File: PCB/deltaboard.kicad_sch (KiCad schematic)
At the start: 316 parts, among them J1 USB_C_Receptacle, J2 Conn_01x04, K1 Esc, K10 F9, K11 F10, K12 F11, K13 F12, K14 Blank, K15 Blank, K16 ~~,`, K17 !,1, K18 @,2, K19 #,3, K2 F1, K20 $,4, K21 %,5, K22 ^,6, K23 &,7, K24 *,8, K25 (,9, K26 ),0, K27 _,-, K28 +,=, K29 Backspace, K3 F2, K30 Insert, K31 Home, K33 Tab, K34 Q, K35 W, K36 E, K37 R, K38 T, K39 Y, K4 F3, K40 U, K41 I, K42 O, K43 P, K44 {,[, K45 },], K46 |,\, K47 Delete, K48 End, K49 PgUp, K5 F4, K50 Caps Lock, K51 A, K52 S, K53 D, K54 F, K55 G, K56 H, K57 J, K58 K, K59 L, K6 F5, K60 :,;, K61 ",', K62 Enter, K63 Shift, K64 Z, K65 X, K66 C, K67 V, K68 B, K69 N, K7 F6, K70 M, K71 <,,, K72 >,., K73 ?,/, K74 Shift, K75 ↑, K76 Ctrl, K77 Win, K78 Alt, K79 Blank, K8 F7, K80 Alt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

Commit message: chore: add i2c pull up resistors and make vcc traces thicker
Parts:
- added R10, R7: 10k, Resistor_SMD:R_0805_2012Metric, symbol Device:R
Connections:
- net +3V3: now also R10.2, R7.2
- net I2C_SCL: now also R10.1
- net I2C_SDA: now also R7.1

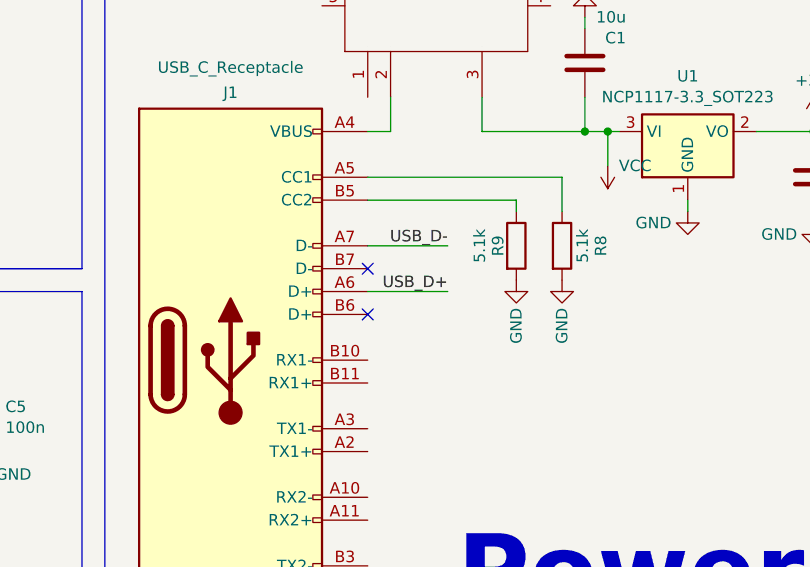
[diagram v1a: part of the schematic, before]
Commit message: chore: properly connect DN/DP
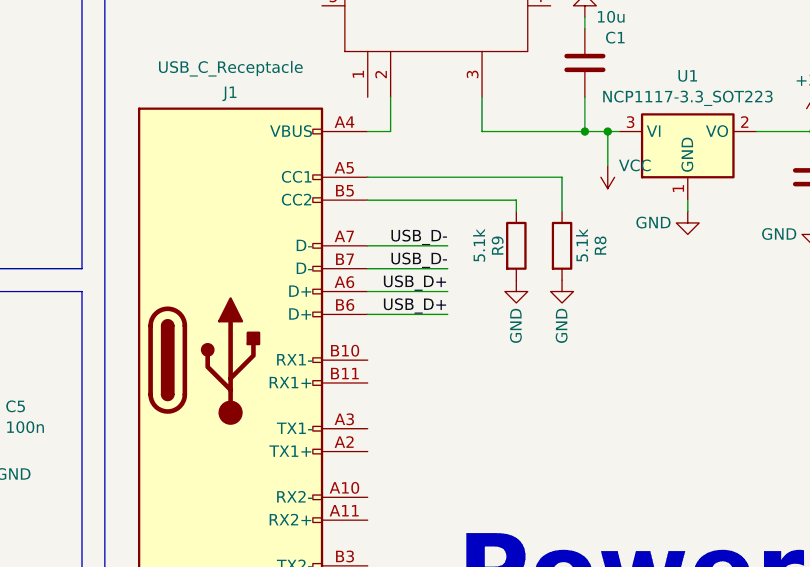
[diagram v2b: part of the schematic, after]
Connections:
- net USB_D+: now also J1.B6 (D+)
- net USB_D-: now also J1.B7 (D-)
- no-connect marks 2 -> 0
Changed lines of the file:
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@@
 		(color 0 0 0 0)
 	)
-	(no_connect
-		(at 521.97 78.74)
-	)
-	(no_connect
-		(at 521.97 83.82)
-	)
 	(wire
 		(pts
@@
 	(wire
 		(pts
+			(xy 521.97 78.74) (xy 530.86 78.74)
+		)
+		(stroke
+			(width 0)
+			(type default)
+		)
+	)
+	(wire
+		(pts
 			(xy 513.08 298.45) (xy 528.32 298.45)
 		)
@@
 	(wire
 		(pts
+			(xy 521.97 83.82) (xy 530.86 83.82)
+		)
+		(stroke
+			(width 0)
+			(type default)
+		)
+	)
+	(wire
+		(pts
 			(xy 434.34 114.3) (xy 438.15 114.3)
 		)
@@
 		)
 	)
+	(label "USB_D+"
+		(at 530.86 83.82 180)
+		(effects
+			(font
+				(size 1.27 1.27)
+			)
+			(justify right bottom)
+		)
+	)
 	(label "ROW_3"
 		(at 196.85 104.14 0)
@@
 		(effects
 			(font
+				(size 1.27 1.27)
+			)
+			(justify right bottom)
+		)
+	)
+	(label "USB_D-"
+		(at 530.86 78.74 180)
+		(effects
+			(font

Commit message: feat: optimize traces, component placement, silkscreen, etc
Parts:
- removed JP1, JP2: Jumper_2_Open, Jumper:SolderJumper-2_P1.3mm_Open_TrianglePad1.0x1.5mm, symbol Jumper:Jumper_2_Open
- added TP_BOOT1, TP_GND1, TP_RST1: TestPoint, TestPoint:TestPoint_Pad_1.5x1.5mm, symbol Connector:TestPoint
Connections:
- net GND: now also SW11.MP, TP_GND1.1
- net ~{USB_BOOT}: now also TP_BOOT1.1
- net at R6.1: now also TP_RST1.1

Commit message: feat: rework component placement + use different vrm fix bugs
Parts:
- removed TP_BOOT1, TP_RST1: TestPoint, TestPoint:TestPoint_Pad_1.5x1.5mm, symbol Connector:TestPoint
- removed U1: NCP1117-3.3_SOT223, Package_TO_SOT_SMD:SOT-223-3_TabPin2, symbol Regulator_Linear:NCP1117-3.3_SOT223
- added D88: PRTR5V0U2X, Package_TO_SOT_SMD:SOT-143, symbol Power_Protection:PRTR5V0U2X
- added J3: Conn_01x06, Connector_PinHeader_2.54mm:PinHeader_1x06_P2.54mm_Vertical, symbol Connector_Generic:Conn_01x06
- added U1: AP2112K-3.3, Package_TO_SOT_SMD:SOT-23-5, symbol Regulator_Linear:AP2112K-3.3
- R6: value 1k -> 10k
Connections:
- net GPIO28_ADC2 is gone; now on net COL_10: U3.40 (GPIO28_ADC2)
- net +3V3: now also R6.1, J3.1 (Pin_1), U1.5 (VOUT)
- net COL_10: no longer U3.27 (GPIO16)
- net GND: now also D88.1 (GND), J3.2 (Pin_2), U1.2 (GND)
- net RUN: now also J3.3 (Pin_3)
- net SWCLK: now also J3.5 (Pin_5)
- net SWD: now also J3.6 (Pin_6)
- net USB_D+: now also D88.3 (I/O2)
- net USB_D-: now also D88.2 (I/O1)
- net VCC: now also U1.1 (VIN), U1.3 (EN)
- net ~{USB_BOOT}: now also J3.4 (Pin_4)
- net VBUS_RAW: now reaches J1.A4 (VBUS), J1.A9 (VBUS), J1.B4 (VBUS), J1.B9 (VBUS), SW1.2
- net VBUS_RAW: now also D88.4 (VCC)
- new net GPIO16: U3.27 (GPIO16)
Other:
- moved on the sheet: R6

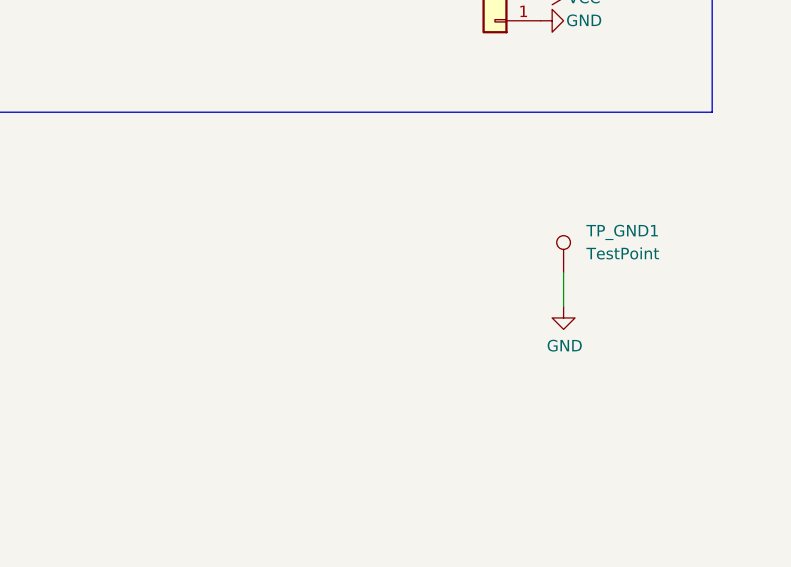
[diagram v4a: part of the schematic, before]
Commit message: feat: hide footprint text for switches
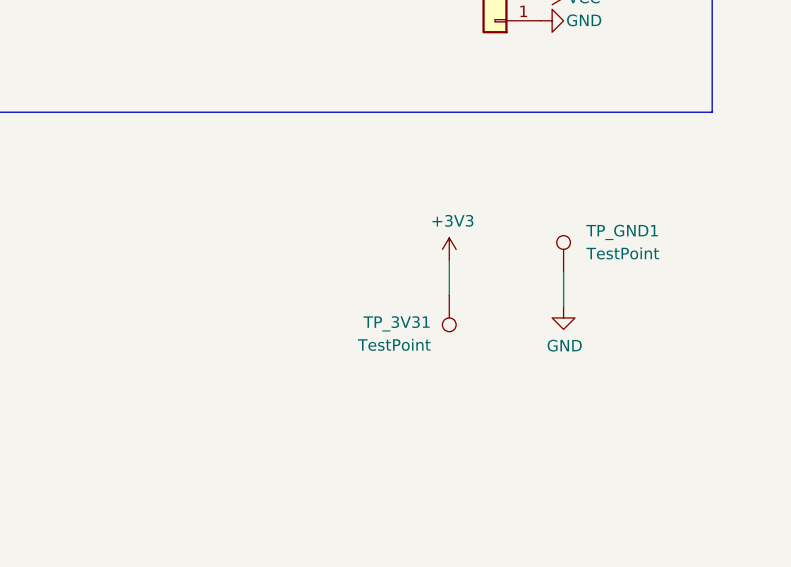
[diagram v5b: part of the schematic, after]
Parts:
- added TP_3V31: TestPoint, TestPoint:TestPoint_Pad_1.5x1.5mm, symbol Connector:TestPoint
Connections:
- net +3V3: now also TP_3V31.1
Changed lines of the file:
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@@
 	(wire
 		(pts
+			(xy 549.91 346.71) (xy 549.91 342.9)
+		)
+		(stroke
+			(width 0)
+			(type default)
+		)
+	)
+	(wire
+		(pts
 			(xy 562.61 257.81) (xy 562.61 260.35)
 		)
@@
 	)
 	(symbol
+		(lib_id "Connector:TestPoint")
+		(at 549.91 346.71 180)
+		(unit 1)
+		(exclude_from_sim no)
+		(in_bom yes)
+		(on_board yes)
+		(dnp no)
+		(property "Reference" "TP_3V31"
+			(at 547.878 349.758 0)
+			(effects
+				(font
+					(size 1.27 1.27)
+				)
+				(justify left)
+			)
+		)
+		(property "Value" "TestPoint"
+			(at 547.878 352.298 0)
+			(effects
+				(font
+					(size 1.27 1.27)
+				)
+				(justify left)
+			)
+		)
+		(property "Footprint" "TestPoint:TestPoint_Pad_1.5x1.5mm"
+			(at 544.83 346.71 0)
+			(effects
+				(font
+					(size 1.27 1.27)
+				)
+				(hide yes)
+			)
+		)
+		(property "Datasheet" "~"
+			(at 544.83 346.71 0)
+			(effects
+				(font
+					(size 1.27 1.27)
+				)
+				(hide yes)
+			)
+		)
+		(property "Description" "test point"
+			(at 549.91 346.71 0)
+			(effects
+				(font
+					(size 1.27 1.27)
+				)
+				(hide yes)
+			)
+		)
+		(pin "1"
+		)
+		(instances
+			(project "deltaboard"
+				(path "/e444e1e5-c848-413e-b43f-8b780f56d443"
+					(reference "TP_3V31")
+					(unit 1)
+				)
+			)
+		)
+	)
+	(symbol
 		(lib_name "GND_2")
 		(lib_id "power:GND")
@@
 					(unit 1)
 				)
+			)
+		)
+	)
+	(symbol
+		(lib_id "power:+3V3")
+		(at 549.91 342.9 0)
+		(unit 1)
+		(exclude_from_sim no)
+		(in_bom yes)
+		(on_board yes)
+		(dnp no)
+		(property "Reference" "#PWR0226"
+			(at 549.91 346.71 0)
+			(effects
+				(font
+					(size 1.27 1.27)
+				)
+				(hide yes)
+			)
+		)
+		(property "Value" "+3V3"
+			(at 550.291 338.5058 0)
+			(effects
+				(font
+					(size 1.27 1.27)
+				)
+			)
+		)
+		(property "Footprint" ""
+			(at 549.91 342.9 0)
+			(effects
+				(font
+					(size 1.27 1.27)
+				)
+				(hide yes)
+			)
+		)
+		(property "Datasheet" ""
+			(at 549.91 342.9 0)
+			(effects
+				(font
+					(size 1.27 1.27)
+				)
+				(hide yes)
+			)
+		)
+		(property "Description" ""
+			(at 549.91 342.9 0)
+			(effects
+				(font
+					(size 1.27 1.27)
+				)
+			)
+		)
+		(pin "1"
+		)
+		(instances
+			(project "deltaboard"
+				(path "/e444e1e5-c848-413e-b43f-8b780f56d443"
+					(reference "#PWR0226")
+					(unit 1)
+				)

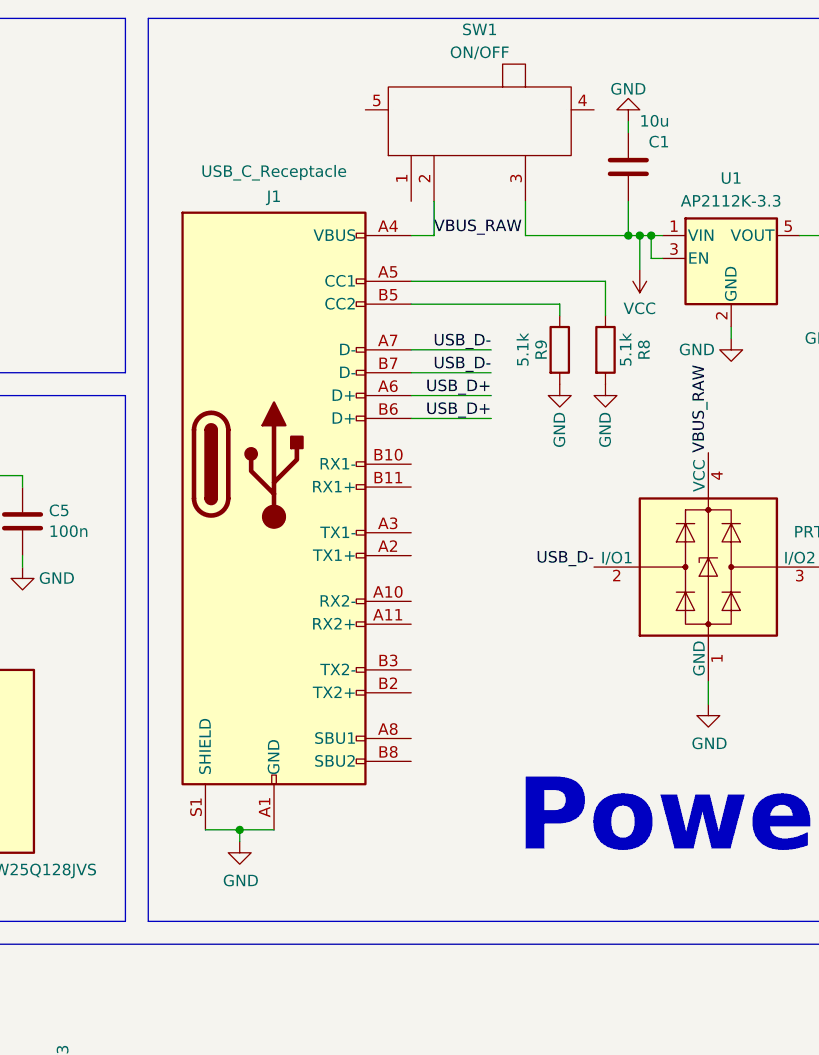
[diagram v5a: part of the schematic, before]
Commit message: chore: fix usb c footprint + symbol
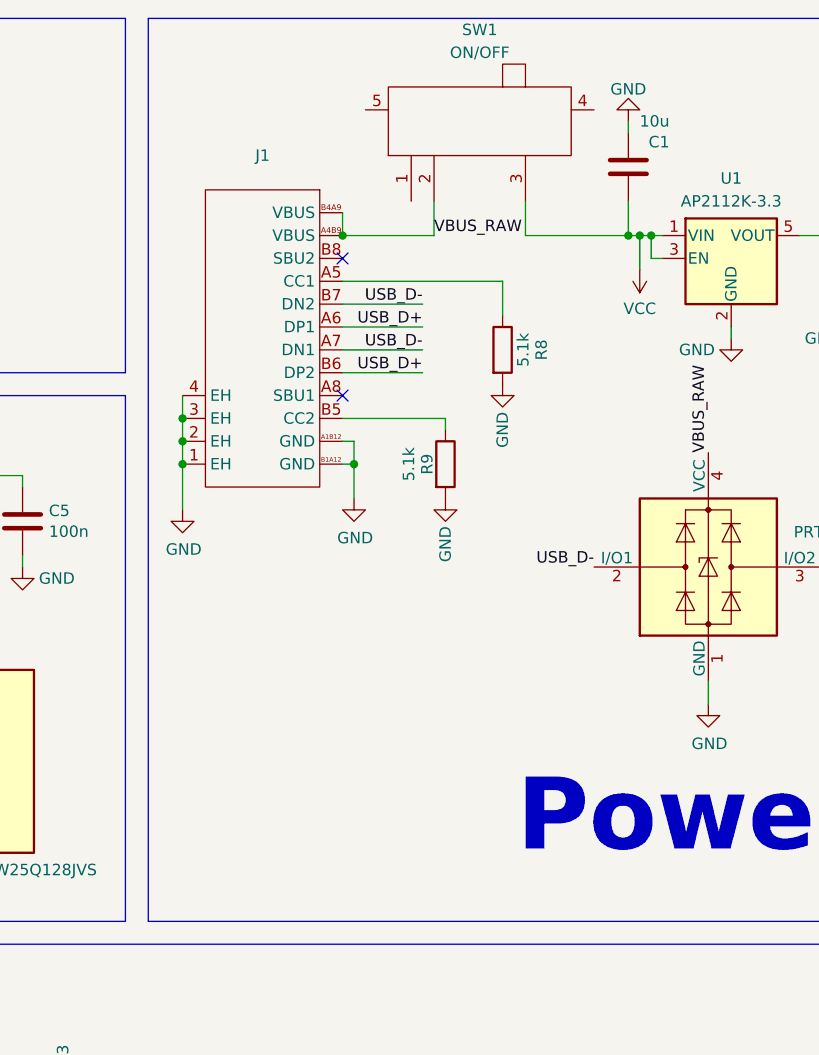
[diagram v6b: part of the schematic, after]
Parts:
- removed J1: USB_C_Receptacle, Components:USB-C_SMD-TYPE-C-31-M-12, symbol Connector:USB_C_Receptacle
- added J1: ~, Components:USB-C_SMD-TYPE-C-31-M-12_1, symbol Components:TYPE-C-31-M-12
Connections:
- net GND: now also J1.1 (EH), J1.2 (EH), J1.3 (EH), J1.4 (EH), J1.A1B12 (GND), J1.B1A12 (GND)
- net USB_D+: now also J1.A6 (DP1), J1.B6 (DP2)
- net USB_D-: now also J1.A7 (DN1), J1.B7 (DN2)
- net VBUS_RAW: now also J1.A4B9 (VBUS), J1.B4A9 (VBUS)
- net at R8.1: now also J1.A5 (CC1)
- net at R9.1: now also J1.B5 (CC2)
- no-connect marks 0 -> 2
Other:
- moved on the sheet: R8, R9

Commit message: feat: use mosfet for switch
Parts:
- added Q1: AO3401A, Package_TO_SOT_SMD:SOT-23, symbol Transistor_FET:AO3401A
- added R11: 10k, Resistor_SMD:R_0402_1005Metric, symbol Device:R
- R10, R7: value 10k -> 2.2k-3.3k
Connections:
- net GND: now also SW1.3
- net VBUS_RAW: now also Q1.2 (S), R11.2; no longer SW1.2
- net VCC: now also Q1.3 (D); no longer SW1.3
- new net: Q1.1 (G), R11.1, SW1.2
- no-connect marks 2 -> 5
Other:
- moved on the sheet: C1, C4, U1
